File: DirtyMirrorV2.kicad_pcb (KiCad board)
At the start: 2 copper layers, 50 x 50 mm, 70 parts, among them J1 PWR, J2 ScopeGroundLoop, SW1 SW_SPDT, U1 TL072, U2 TL074, U3 TL074

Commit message: component layout
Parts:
- added J3: Power, Connector_BarrelJack:BarrelJack_Horizontal, F.Cu at (34.6, 56.0)
- added R35: 1M, Resistor_SMD:R_0805_2012Metric, B.Cu at (5.62, 43.0)
- C2: value 100u -> 10u
- C6: value 2n2 -> 1n
- J1: moved to F.Cu
- J2: value ScopeGroundLoop -> ~; footprint Connector_Pin:THT_GND_WIRE -> Connector:BatteryContact_Keystone_243; moved to F.Cu
- R10, R7: value 51k -> 56k
- R16, R18: value 39k -> 47k
- R19: value 18k -> 22k
- R3: value 22k -> 4k7
- R5: value 33k -> 47k
- SW1: footprint Connector_PinSocket_2.54mm:PinSocket_1x03_P2.54mm_Vertical -> Button_Switch_THT:Toggle_Dailywell_SubMini_SPDT; moved to F.Cu
- TP10: moved to B.Cu
- moved J2 48.4 mm to (-1.46, 55.8), turned to -90 degrees
- moved C2 40.1 mm to (27.1, 35.1), turned to 90 degrees
- moved R15 34.5 mm to (31.6, 37.4)
- moved R19 33.5 mm to (19.5, 41.3), turned to 0 degrees
- moved C7 30.8 mm to (19.7, 39.0), turned to 0 degrees
- moved TP5 28.2 mm to (16.8, 47.4), turned to 180 degrees
- moved R27 26.9 mm to (26.9, 75.5), turned to -90 degrees
- moved R33 25.1 mm to (32.5, 40.2), turned to 90 degrees
- moved R10 24.7 mm to (2.23, 58.7), turned to -90 degrees
- moved R24 24.5 mm to (20.6, 46.5), turned to -90 degrees
- moved TP1 24.1 mm to (11.6, 47.0)
- moved C6 23.7 mm to (19.5, 43.5)
- moved R32 23.4 mm to (32.6, 72.0), turned to 90 degrees
- moved C8 23.2 mm to (26.8, 72.0), turned to -90 degrees
- moved R25 22.8 mm to (20.6, 50.3), turned to -90 degrees
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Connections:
- C3 pad 2: Net-(C3-Pad2) -> Net-(U1A-+)
- C6 pad 1: Net-(U3A-+) -> Net-(U3D-+)
- J1 pad 3: +9V -> /Low_In
- R19 pad 2: Net-(U3A-+) -> Net-(U3D-+)
- R30 pad 2: Net-(U3D--) -> Net-(U3A--)
- R31 pad 2: Net-(U3D--) -> Net-(U3A--)
- R33 pad 1: Net-(U3D--) -> Net-(U3A--)
- R5 pad 1: Net-(C3-Pad2) -> /Bias
- U1 pad 3: /Bias -> Net-(U1A-+)
- U3 pad 1: /FxFull -> /FxRaw
- U3 pad 12: /Bias -> Net-(U3D-+)
- U3 pad 13: Net-(U3D--) -> /FxFull
- U3 pad 14: /FxRaw -> /FxFull
- U3 pad 2: /FxFull -> Net-(U3A--)
- U3 pad 3: Net-(U3A-+) -> /Bias
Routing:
- net +9V: track 132.6 -> 0.00 mm, vias 3 -> 0
- net /Bias: track 94.1 -> 0.00 mm, vias 3 -> 0
- net /FxFull: track 64.3 -> 0.00 mm, vias 1 -> 0
- net /Gain: track 56.0 -> 0.00 mm, vias 3 -> 0
- net /HiRect: track 45.5 -> 0.00 mm, vias 2 -> 0
- net Net-(SW1-B): track 41.2 -> 0.00 mm
- net Net-(U3C--): track 39.6 -> 0.00 mm, vias 2 -> 0
- net FX_IN: track 36.0 -> 0.00 mm
- net /Clip: track 31.0 -> 0.00 mm
- net Net-(U3D--): track 30.5 -> 0.00 mm, vias 2 -> 0
- net /Fold: track 29.8 -> 0.00 mm
- net Net-(U3B--): track 24.8 -> 0.00 mm
- net /HiThresh: track 24.0 -> 0.00 mm, vias 1 -> 0
- net /LoRect: track 20.1 -> 0.00 mm, vias 2 -> 0
- net /Byp: track 19.4 -> 0.00 mm
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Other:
- board size 50 x 50 mm -> 54 x 57.9 mm
- board text removed: "+9v"
- board text removed: "GND"
- board text removed: "Gain"
- board text removed: "In"
- board text removed: "Out"
- board text removed: "Shape"
- board text removed: "Tone"
- board text removed: "Volume"

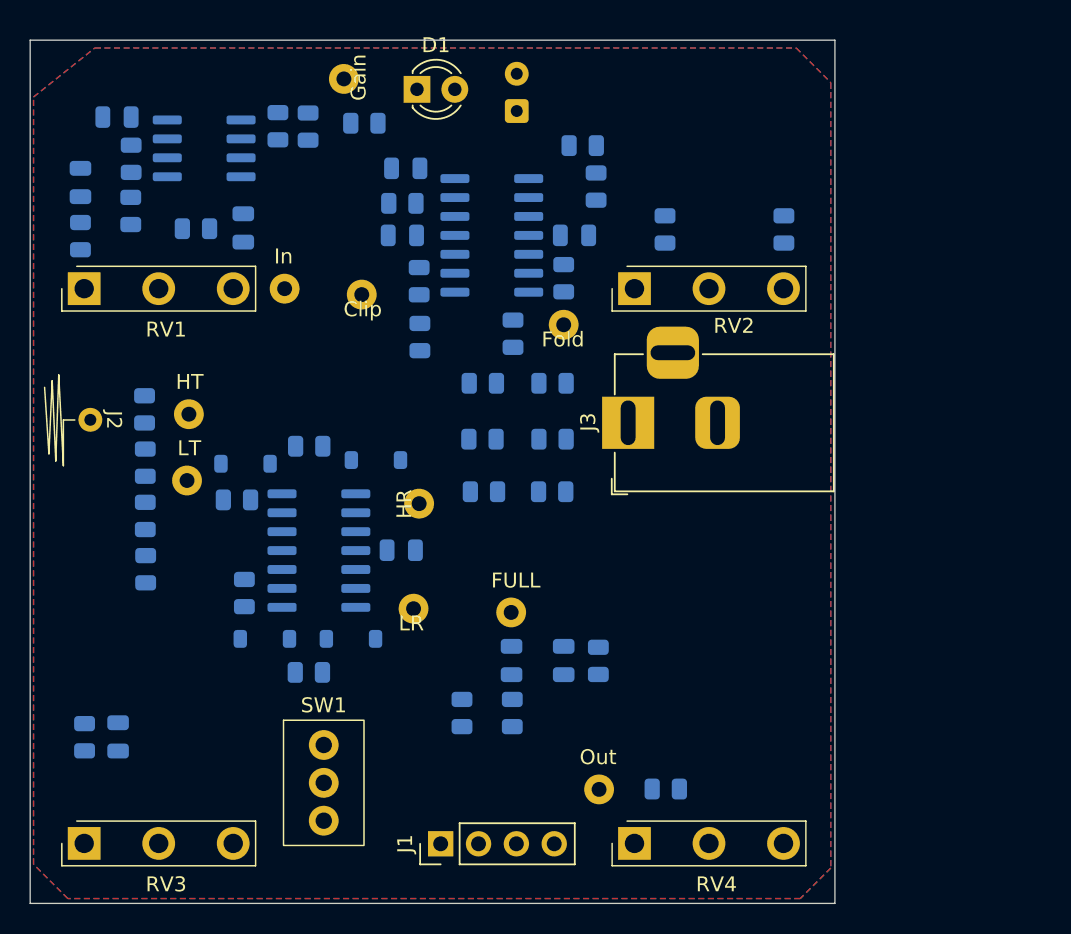
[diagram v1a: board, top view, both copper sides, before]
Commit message: prelim routed, DRC passing
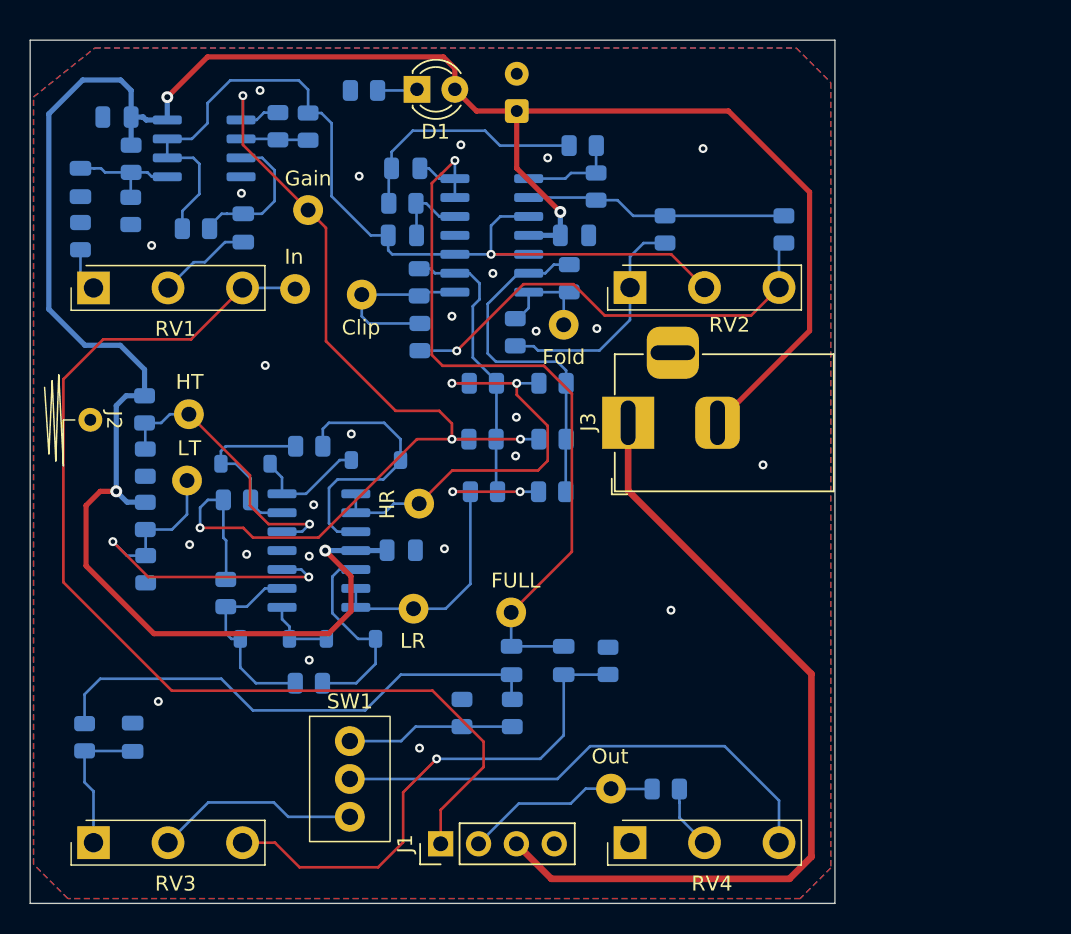
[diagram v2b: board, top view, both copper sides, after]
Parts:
- moved TP7 9.12 mm to (13.2, 41.8), turned to 0 degrees
- moved R4 2.20 mm to (16.9, 33.7)
- moved SW1 1.77 mm to (15.9, 79.9)
- moved R11 1.25 mm to (7.62, 67.5)
- moved C10 0.98 mm to (1.38, 77.1)
- moved TP10 0.80 mm to (33.5, 80.6)
- moved R13 0.72 mm to (13.2, 73.5)
- moved TP1 0.70 mm to (12.3, 47.0)
- moved R32 0.65 mm to (33.3, 72.0)
- moved RV1 0.63 mm to (-1.25, 47.0)
- moved RV3 0.63 mm to (-1.25, 84.2)
- moved R23 0.38 mm to (30.7, 46.3)
- moved RV2 0.31 mm to (34.8, 47.0)
- moved RV4 0.30 mm to (34.8, 84.2)
- moved R26 0.18 mm to (27.1, 50.0)
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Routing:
- net +9V: track 0.00 -> 161.8 mm, vias 0 -> 4
- net FX_IN: track 0.00 -> 72.4 mm
- net /Gain: track 0.00 -> 70.4 mm, vias 0 -> 4
- net /Bias: track 0.00 -> 64.2 mm, vias 0 -> 1
- net /Low_In: track 0.00 -> 55.6 mm
- net /FxFull: track 0.00 -> 51.5 mm, vias 0 -> 1
- net /HiPass: track 0.00 -> 34.9 mm, vias 0 -> 1
- net Net-(C8-Pad2): track 0.00 -> 34.6 mm
- net Net-(SW1-B): track 0.00 -> 34.0 mm
- net Net-(R25-Pad2): track 0.00 -> 30.7 mm, vias 0 -> 1
- net /HiRect: track 0.00 -> 28.6 mm, vias 0 -> 2
- net /LoThresh: track 0.00 -> 26.0 mm, vias 0 -> 2
- net Net-(U3B--): track 0.00 -> 23.8 mm
- net /LoRect: track 0.00 -> 22.8 mm, vias 0 -> 2
- net /HiThresh: track 0.00 -> 19.4 mm, vias 0 -> 1
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
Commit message: moved bulk capacitor, silkscreen
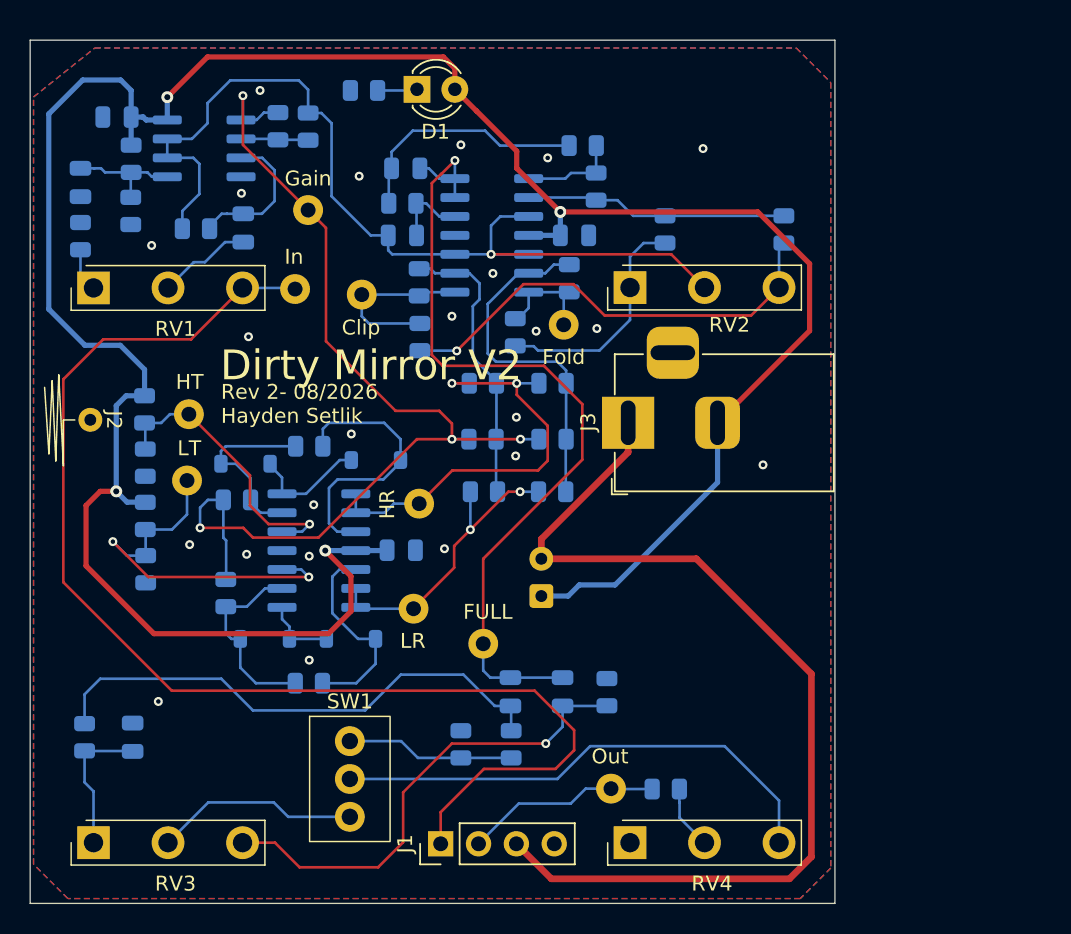
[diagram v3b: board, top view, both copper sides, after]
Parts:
- moved C2 32.6 mm to (28.8, 67.7)
- moved TP6 2.82 mm to (24.9, 70.8)
- moved C8 2.10 mm to (26.7, 74.1)
- moved C9 2.10 mm to (30.2, 74.1)
- moved R27 2.10 mm to (26.8, 77.6)
- moved R28 2.10 mm to (23.4, 77.6)
- moved R32 2.10 mm to (33.2, 74.1)
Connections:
- C2 pad 2: 0 -> /Low_In
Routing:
- net FX_IN: track 72.4 -> 84.3 mm
- net /Low_In: track 55.6 -> 66.5 mm
- net +9V: track 161.8 -> 170.7 mm
- net /FxFull: track 51.5 -> 56.4 mm
- net /LoRect: track 22.8 -> 20.2 mm
- net /HiPass: track 34.9 -> 32.4 mm
- net Net-(C8-Pad2): track 34.6 -> 35.4 mm
- net 0: vias 25 -> 23
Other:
- board text added: "Rev 2- 08/2026 Hayden Setlik"
- board text removed: "Rev 1- 02/2026 Hayden Setlik"

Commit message: new power scheme routed
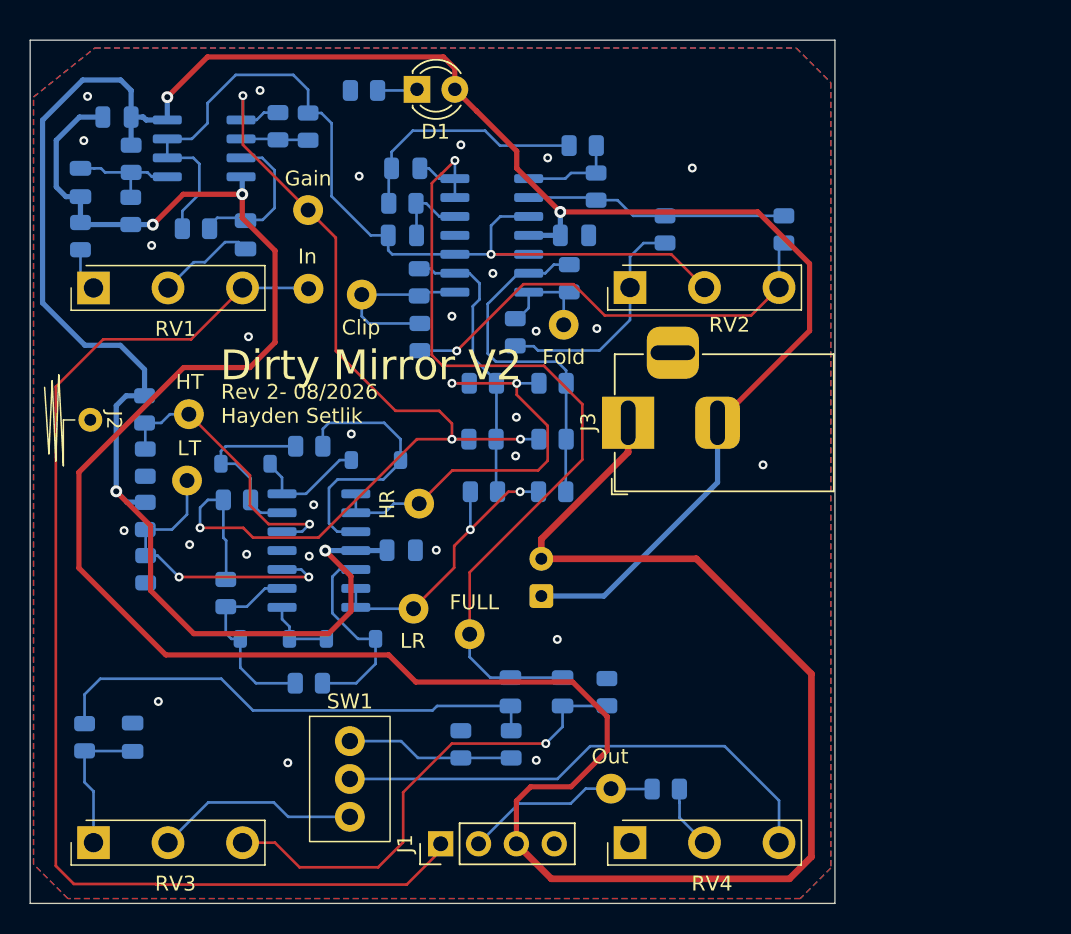
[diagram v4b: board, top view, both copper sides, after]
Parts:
- C3: value 1u -> 100n
- R35: value 1M -> 470k
- moved TP6 1.11 mm to (24.0, 70.2)
- moved TP1 0.91 mm to (13.2, 47.0)
- moved C3 0.48 mm to (8.95, 43.4)
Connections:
- net Net-(U1A-+) renamed /InputBiased
- C1 pad 2: 0 -> /Low_In
- C4 pad 2: 0 -> /Low_In
- R2 pad 2: 0 -> /Low_In
- R3 pad 2: 0 -> /Low_In
- U1 pad 4: 0 -> /Low_In
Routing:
- net /Low_In: track 66.5 -> 176.3 mm, vias 0 -> 2
- net /LoThresh: track 26.0 -> 20.8 mm
- net FX_IN: track 84.3 -> 79.6 mm
- net +9V: track 170.7 -> 167.2 mm
- net Net-(C8-Pad2): track 35.4 -> 33.7 mm
- net /FxFull: track 56.4 -> 57.2 mm
- net /InputBiased: track 9.91 -> 10.5 mm
- net 0: vias 23 -> 27

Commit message: moved gain control to feedback loop
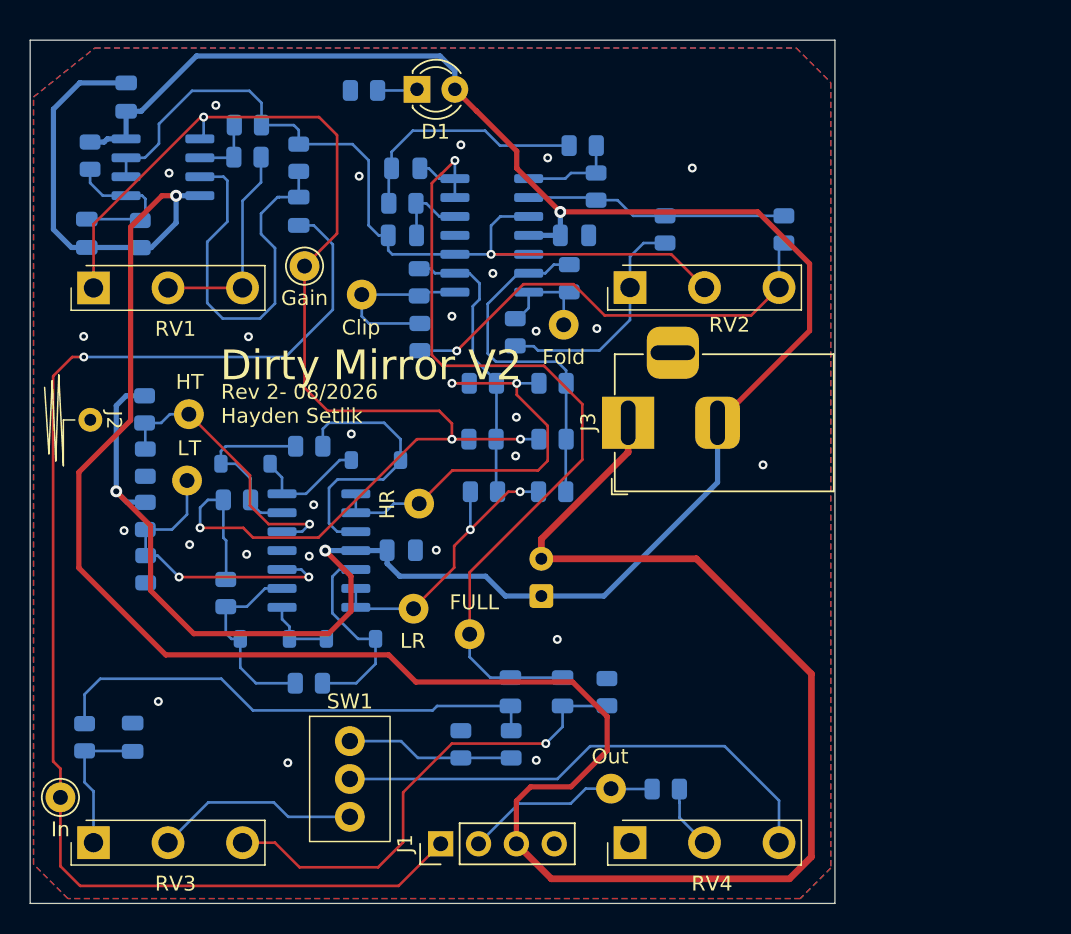
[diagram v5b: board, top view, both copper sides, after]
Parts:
- removed R3: 4k7, Resistor_SMD:R_0805_2012Metric
- R5: value 47k -> 4k7
- R6: value 1M -> 220R
- TP1, TP7: moved to F.Cu
- moved TP1 38.0 mm to (-3.47, 81.2)
- moved R35 8.38 mm to (12.5, 38.2), turned to 90 degrees
- moved R5 4.04 mm to (9.11, 36.0), turned to 180 degrees
- moved C3 3.90 mm to (12.5, 41.8)
- moved TP7 3.77 mm to (12.9, 45.5)
- moved C1 3.44 mm to (-1.70, 43.3)
- moved U1 3.04 mm to (3.41, 38.9)
- moved R6 2.91 mm to (9.08, 38.2), turned to 0 degrees
- moved R1 2.76 mm to (-1.48, 38.1)
- moved R2 1.68 mm to (1.89, 43.4)
- moved C4 1.47 mm to (0.94, 34.2), turned to 90 degrees
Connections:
- C3 pad 1: Net-(C3-Pad1) -> FX_IN
- R6 pad 2: /Gain -> Net-(R6-Pad2)
- RV1 pad 1: Net-(R3-Pad1) -> /Gain
- RV1 pad 2: Net-(C3-Pad1) -> Net-(R6-Pad2)
- RV1 pad 3: FX_IN -> Net-(R6-Pad2)
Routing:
- net /Gain: track 70.4 -> 90.9 mm
- net +9V: track 167.2 -> 149.0 mm, vias 4 -> 3
- net /InputBiased: track 10.5 -> 27.3 mm
- net Net-(R6-Pad2): track 0.00 -> 14.3 mm
- net FX_IN: track 79.6 -> 88.6 mm, vias 0 -> 1
- net Net-(C3-Pad1): track 6.66 -> 0.00 mm
- net /Bias: track 64.5 -> 60.0 mm
- net Net-(R3-Pad1): track 2.92 -> 0.00 mm
- net /Low_In: track 176.3 -> 173.5 mm, vias 2 -> 1
- net Net-(U1B-+): track 7.74 -> 10.3 mm
- net 0: vias 27 -> 26

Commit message: grounding tweaks and corner bevels
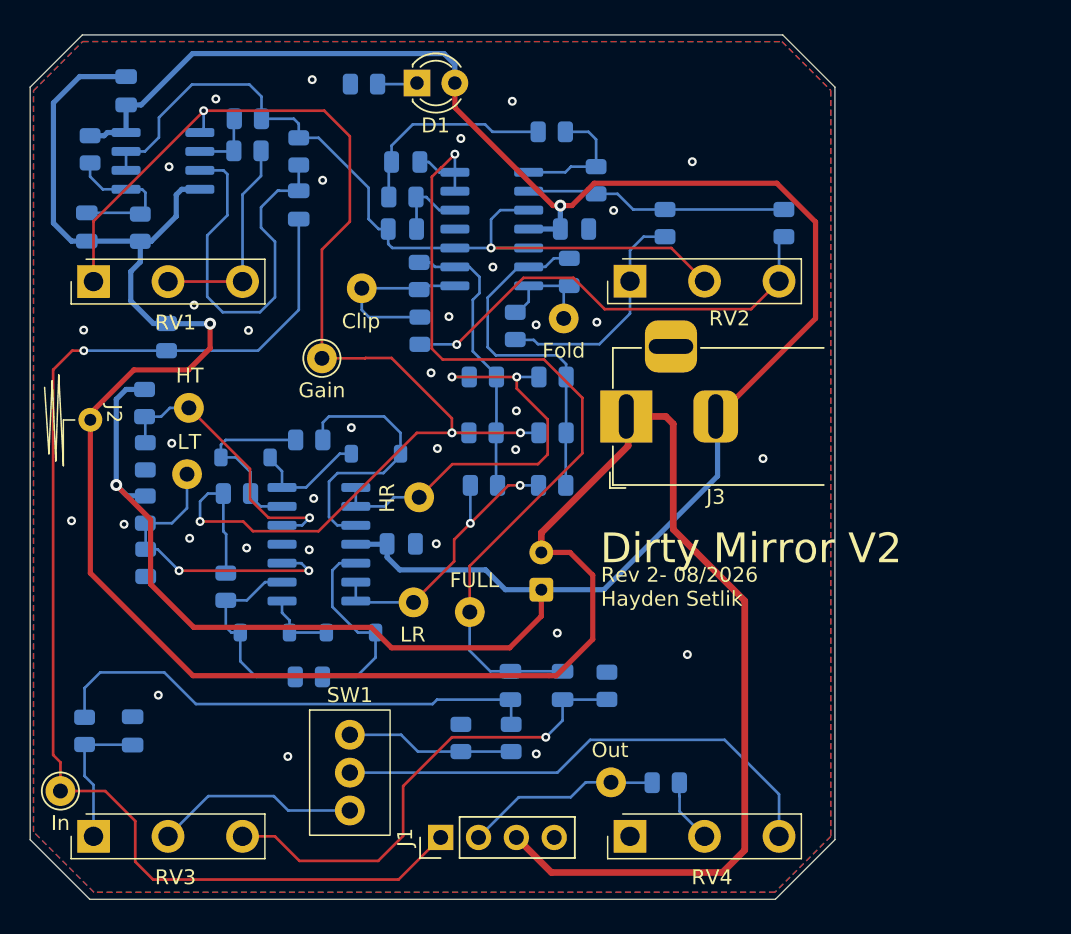
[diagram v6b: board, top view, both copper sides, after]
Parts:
- added R36: 1Meg, Resistor_SMD:R_0805_2012Metric, B.Cu at (3.65, 50.3)
- R35: value 470k -> 1Meg
- moved TP7 6.30 mm to (14.1, 51.7)
- moved R15 2.27 mm to (29.5, 36.5)
- moved TP6 1.49 mm to (24.0, 68.7)
- moved J3 0.44 mm to (34.5, 55.6)
- moved C2 0.43 mm to (28.8, 67.2)
- moved D2 0.43 mm to (10.2, 70.1)
- moved D4 0.43 mm to (16.0, 70.1)
- moved J1 0.43 mm to (22.0, 83.8)
- moved C1 0.43 mm to (-1.70, 42.9)
- moved C4 0.43 mm to (0.94, 33.7)
- moved C6 0.43 mm to (19.5, 43.0)
- moved C7 0.43 mm to (19.7, 38.5)
- moved R1 0.43 mm to (-1.48, 37.7)
- moved R10 0.43 mm to (2.23, 58.3)
- moved R14 0.43 mm to (13.2, 57.2)
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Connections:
- J2 pad 1: 0 -> /Low_In
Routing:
- net +9V: track 149.0 -> 161.0 mm, vias 3 -> 2
- net /Low_In: track 173.5 -> 167.2 mm
- net FX_IN: track 88.6 -> 83.9 mm
- net Net-(C7-Pad1): track 16.4 -> 14.2 mm
- net /FxRaw: track 6.52 -> 8.78 mm
- net /Gain: track 90.9 -> 89.1 mm
- net /Bias: track 60.0 -> 58.7 mm
- net 0: vias 26 -> 34
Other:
- board size 54 x 57.9 mm -> 54 x 58 mm

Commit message: rev2 sent to fab
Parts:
- SW1: footprint Button_Switch_THT:Toggle_Dailywell_SubMini_SPDT -> Button_Switch_THT:SW_SPDT_Dailywell_Mini_1M
- moved TP7 15.4 mm to (-1.25, 49.8)
- moved SW1 8.97 mm to (13.4, 70.9)
- moved C5 4.52 mm to (20.3, 59.7)
- moved D3 4.52 mm to (9.88, 53.9)
- moved D5 4.52 mm to (18.6, 53.7)
- moved R11 4.52 mm to (8.55, 62.6)
- moved R12 4.52 mm to (9.30, 56.3)
- moved TP4 4.52 mm to (21.1, 63.6)
- moved D2 4.52 mm to (11.2, 65.7)
- moved D4 4.52 mm to (16.9, 65.7)
- moved R13 4.52 mm to (14.1, 68.7)
- moved R14 4.52 mm to (14.2, 52.8)
- moved U2 4.52 mm to (14.8, 59.8)
- moved TP2 4.52 mm to (21.5, 56.6)
- moved C2 2.41 mm to (27.4, 65.3), turned to 0 degrees
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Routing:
- net /Low_In: track 167.2 -> 120.7 mm
- net +9V: track 161.0 -> 193.3 mm, vias 2 -> 4
- net /Gain: track 89.1 -> 66.5 mm
- net /InputBiased: track 27.3 -> 10.5 mm
- net /HiRect: track 28.6 -> 20.0 mm
- net /HiPass: track 32.4 -> 38.1 mm, vias 1 -> 0
- net /HiThresh: track 19.4 -> 14.8 mm, vias 1 -> 0
- net /Bias: track 58.7 -> 62.6 mm
- net /LoThresh: track 20.8 -> 17.4 mm, vias 2 -> 0
- net FX_IN: track 83.9 -> 86.8 mm, vias 1 -> 0
- net /Byp: track 11.3 -> 14.1 mm
- net /Tone: track 13.7 -> 16.6 mm
- net Net-(U3B--): track 23.8 -> 21.4 mm
- net /FxFull: track 57.2 -> 54.9 mm, vias 1 -> 2
- net /LoRect: track 20.2 -> 18.2 mm, vias 2 -> 0
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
